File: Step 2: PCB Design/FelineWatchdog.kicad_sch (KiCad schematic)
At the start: 32 parts, among them J1 USB_C_Receptacle_PowerOnly_6P, J12 Conn_01x04_Socket, J2 Conn_01x02_Socket, J3 Conn_01x02_Pin, J9 USB_B_Micro, Q2 FS8205A, SW1 RESET, U1 AMS1117-3.3, U3 TP4056, U4 DW01A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

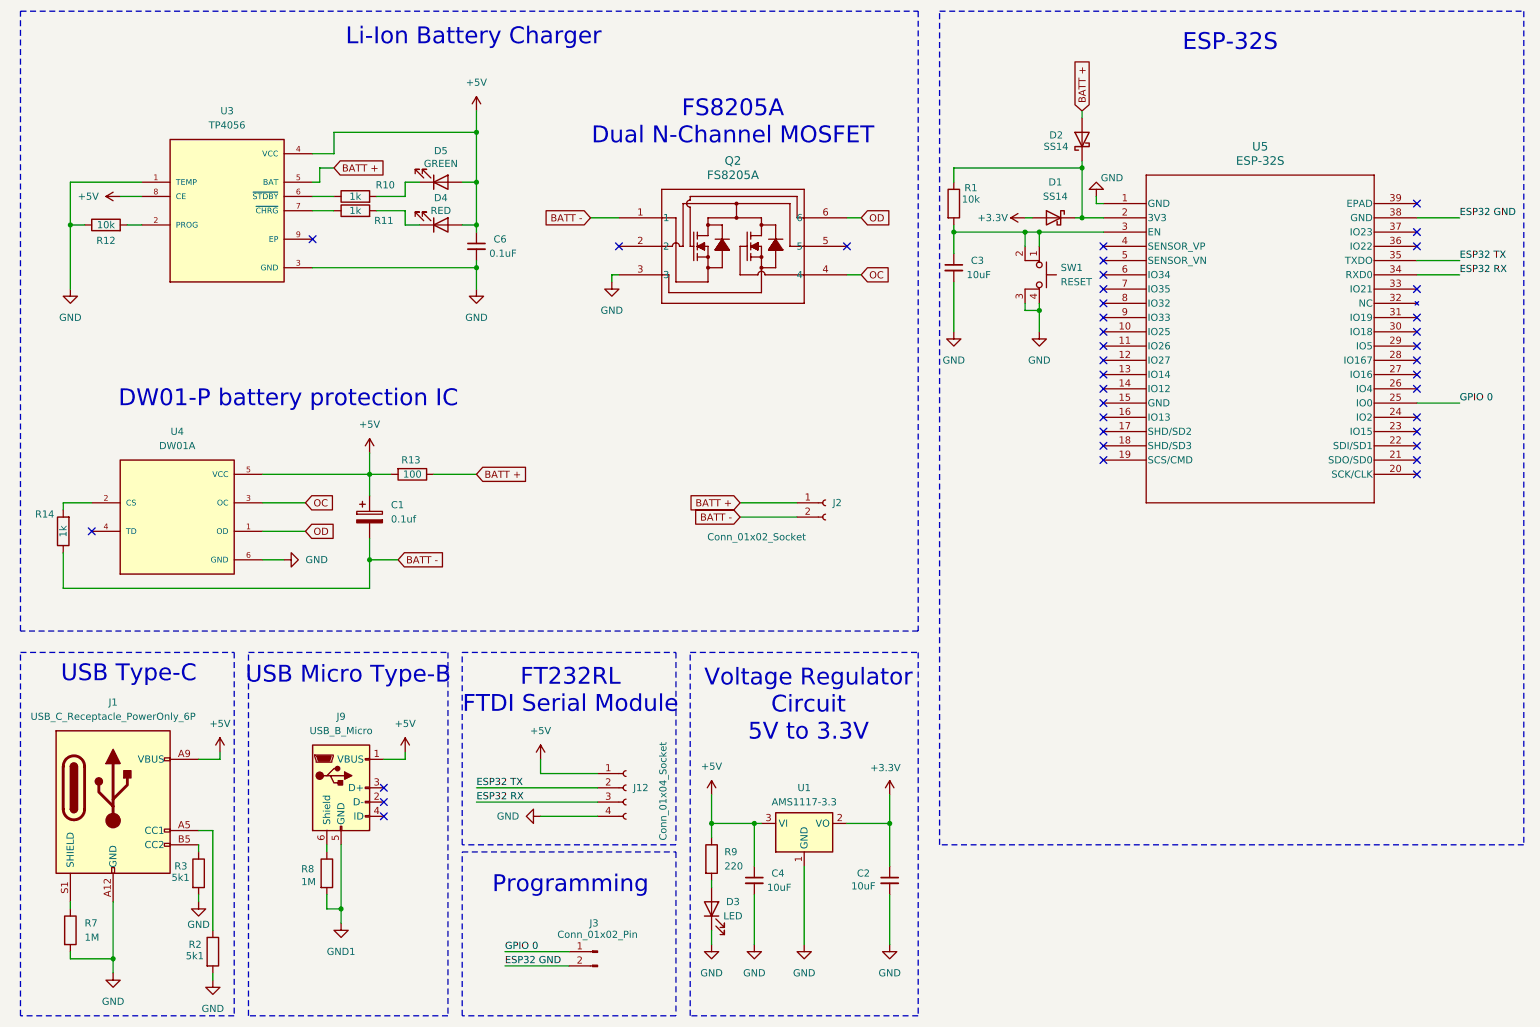
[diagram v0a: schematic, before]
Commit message: Switch to 4-layer PCB stackup with dedicated power and ground planes Inner layers ensure stable power delivery, improved signal integrity, and reduced EMI.
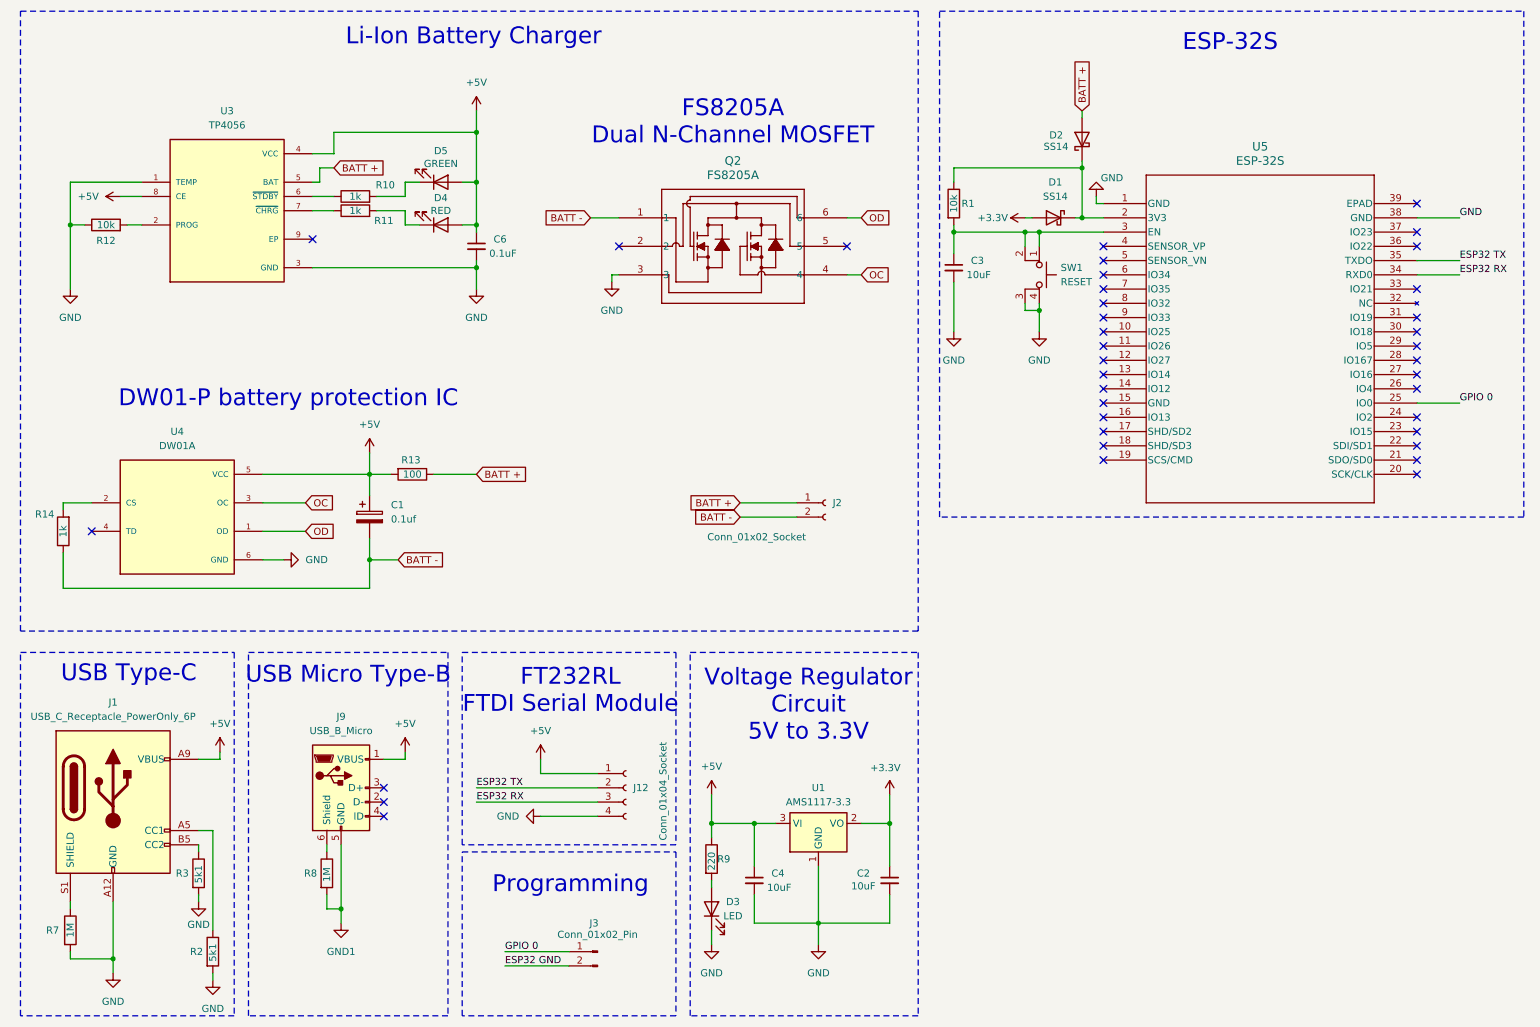
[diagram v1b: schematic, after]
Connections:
- net ESP32 GND: no longer U5.38 (GND)
- net GND: now also U5.38 (GND)
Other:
- moved on the sheet: U1
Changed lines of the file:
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@@
 	)
 	(junction
+		(at 156.21 177.8)
+		(diameter 0)
+		(color 0 0 0 0)
+	)
+	(junction
 		(at 30.48 184.15)
 		(diameter 0)
@@
 	(wire
 		(pts
+			(xy 168.91 172.72) (xy 168.91 177.8)
+		)
+		(stroke
+			(width 0)
+			(type default)
+		)
+	)
+	(wire
+		(pts
 			(xy 66.04 60.96) (xy 95.25 60.96)
 		)
@@
 	(wire
 		(pts
-			(xy 144.78 160.02) (xy 146.05 160.02)
+			(xy 144.78 160.02) (xy 148.59 160.02)
 		)
 		(stroke
@@
 	(wire
 		(pts
-			(xy 153.67 167.64) (xy 153.67 181.61)
+			(xy 156.21 167.64) (xy 156.21 177.8)
 		)
 		(stroke
@@
 	(wire
 		(pts
-			(xy 168.91 172.72) (xy 168.91 181.61)
+			(xy 156.21 177.8) (xy 168.91 177.8)
 		)
 		(stroke
@@
 	(wire
 		(pts
+			(xy 156.21 177.8) (xy 156.21 181.61)
+		)
+		(stroke
+			(width 0)
+			(type default)
+		)
+	)
+	(wire
+		(pts
+			(xy 144.78 172.72) (xy 144.78 177.8)
+		)
+		(stroke
+			(width 0)
+			(type default)
+		)
+	)
+	(wire
+		(pts
 			(xy 195.58 54.61) (xy 207.01 54.61)
 		)
@@
 	(wire
 		(pts
-			(xy 161.29 160.02) (xy 168.91 160.02)
+			(xy 163.83 160.02) (xy 168.91 160.02)
 		)
 		(stroke
@@
 	(wire
 		(pts
-			(xy 95.25 53.34) (xy 95.25 45.72)
+			(xy 144.78 177.8) (xy 156.21 177.8)
 		)
 		(stroke
@@
 	(wire
 		(pts
-			(xy 92.71 45.72) (xy 95.25 45.72)
+			(xy 95.25 53.34) (xy 95.25 45.72)
 		)
 		(stroke
@@
 	(wire
 		(pts
-			(xy 66.04 48.26) (xy 69.85 48.26)
+			(xy 92.71 45.72) (xy 95.25 45.72)
 		)
 		(stroke
@@
 	(wire
 		(pts
-			(xy 144.78 172.72) (xy 144.78 181.61)
+			(xy 66.04 48.26) (xy 69.85 48.26)
 		)
 		(stroke
@@
 	(rectangle
 		(start 177.8 15.24)
-		(end 281.94 163.83)
+		(end 281.94 105.41)
 		(stroke
 			(width 0)
@@
 		)
 	)
-	(label "ESP32 GND"
-		(at 270.51 52.07 0)
-		(fields_autoplaced yes)
-		(effects
-			(font
-				(size 1.27 1.27)
-			)
-			(justify left bottom)
-		)
-	)
 	(label "ESP32 TX"
 		(at 95.25 153.67 0)
@@
 		)
 	)
+	(label "GND"
+		(at 270.51 52.07 0)
+		(fields_autoplaced yes)
+		(effects
+			(font
+				(size 1.27 1.27)
+			)
+			(justify left bottom)
+		)
+	)
 	(global_label "BATT +"
 		(shape input)
@@
 		(on_board yes)
 		(dnp no)
-		(fields_autoplaced yes)
 		(property "Reference" "R7"
-			(at 25.4 177.7999 0)
+			(at 18.542 179.07 0)
 			(effects
 				(font
@@
 		)
 		(property "Value" "1M"
-			(at 25.4 180.3399 0)
+			(at 22.86 180.34 90)
 			(effects
 				(font
@@
 	(symbol
 		(lib_id "power:GND")
-		(at 153.67 181.61 0)
+		(at 156.21 181.61 0)
 		(unit 1)
 		(exclude_from_sim no)
@@
 		(fields_autoplaced yes)
 		(property "Reference" "#PWR012"
-			(at 153.67 187.96 0)
+			(at 156.21 187.96 0)
 			(effects
 				(font
@@
 		)
 		(property "Value" "GND"
-			(at 153.67 186.69 0)
+			(at 156.21 186.69 0)
 			(effects
 				(font
@@
 		)
 		(property "Footprint" ""
-			(at 153.67 181.61 0)
+			(at 156.21 181.61 0)
 			(effects
 				(font
@@
 		)
 		(property "Datasheet" ""
-			(at 153.67 181.61 0)
+			(at 156.21 181.61 0)
 			(effects
 				(font
@@
 		)
 		(property "Description" "Power symbol creates a global label with name \"GND\" , ground"
-			(at 153.67 181.61 0)
+			(at 156.21 181.61 0)
 			(effects
 				(font
@@
 	)
 	(symbol
-		(lib_id "power:GND")
-		(at 144.78 181.61 0)
-		(unit 1)
-		(exclude_from_sim no)
-		(in_bom yes)
-		(on_board yes)
-		(dnp no)
-		(fields_autoplaced yes)
-		(property "Reference" "#PWR011"
-			(at 144.78 187.96 0)
-			(effects
-				(font
-					(size 1.27 1.27)
-				)
-				(hide yes)
-			)
-		)
-		(property "Value" "GND"
-			(at 144.78 186.69 0)
-			(effects
-				(font
-					(size 1.27 1.27)
-				)
-			)
-		)
-		(property "Footprint" ""
-			(at 144.78 181.61 0)
-			(effects
-				(font
-					(size 1.27 1.27)
-				)
-				(hide yes)
-			)
-		)
-		(property "Datasheet" ""
-			(at 144.78 181.61 0)
-			(effects
-				(font
-					(size 1.27 1.27)
-				)
-				(hide yes)
-			)
-		)
-		(property "Description" "Power symbol creates a global label with name \"GND\" , ground"
-			(at 144.78 181.61 0)
-			(effects
-				(font
-					(size 1.27 1.27)
-				)
-				(hide yes)
-			)
-		)
-		(pin "1"
-		)
-		(instances
-			(project "FelineWatchdog"
-				(path "/8c4adf75-2d7a-4707-8808-772a211f889e"
-					(reference "#PWR011")
-					(unit 1)
-				)
-			)
-		)
-	)
-	(symbol
 		(lib_id "Device:R")
 		(at 73.66 48.26 90)
@@
 	(symbol
 		(lib_id "Regulator_Linear:AMS1117-3.3")
-		(at 153.67 160.02 0)
+		(at 156.21 160.02 0)
 		(unit 1)
 		(exclude_from_sim no)
@@
 		(fields_autoplaced yes)
 		(property "Reference" "U1"
-			(at 153.67 153.67 0)
+			(at 156.21 153.67 0)
 			(effects
 				(font
@@
 		)
 		(property "Value" "AMS1117-3.3"
-			(at 153.67 156.21 0)
+			(at 156.21 156.21 0)
 			(effects
 				(font
@@
 		)
 		(property "Footprint" "Package_TO_SOT_SMD:SOT-223-3_TabPin2"
-			(at 153.67 154.94 0)
+			(at 156.21 154.94 0)
 			(effects
 				(font
@@
 		)
 		(property "Datasheet" "http://www.advanced-monolithic.com/pdf/ds1117.pdf"
-			(at 156.21 166.37 0)
+			(at 158.75 166.37 0)
 			(effects
 				(font
@@
 		)
 		(property "Description" "1A Low Dropout regulator, positive, 3.3V fixed output, SOT-223"
-			(at 153.67 160.02 0)
+			(at 156.21 160.02 0)
 			(effects
 				(font
@@
 		(dnp no)
 		(property "Reference" "R2"
-			(at 43.942 181.61 0)
+			(at 44.196 182.88 0)
 			(effects
 				(font
@@
 		)
 		(property "Value" "5k1"
-			(at 43.434 183.642 0)
+			(at 48.26 184.658 90)
 			(effects
 				(font
@@
 		(dnp no)
 		(property "Reference" "R3"
-			(at 41.402 167.64 0)
+			(at 41.656 168.91 0)
 			(effects
 				(font
@@
 		)
 		(property "Value" "5k1"
-			(at 40.894 169.672 0)
+			(at 45.72 170.688 90)
 			(effects
 				(font
@@
 		(dnp no)
 		(property "Reference" "R9"
-			(at 139.446 165.1 0)
+			(at 138.176 166.37 0)
 			(effects
 				(font
@@
 		)
 		(property "Value" "220"
-			(at 139.446 167.64 0)
+			(at 137.16 168.402 90)
 			(effects
 				(font
@@
 	)
 	(symbol
-		(lib_id "power:GND")
-		(at 168.91 181.61 0)
-		(unit 1)
-		(exclude_from_sim no)
-		(in_bom yes)
-		(on_board yes)
-		(dnp no)
-		(fields_autoplaced yes)
-		(property "Reference" "#PWR025"
-			(at 168.91 187.96 0)
-			(effects
-				(font
-					(size 1.27 1.27)
-				)
-				(hide yes)
-			)
-		)
-		(property "Value" "GND"
-			(at 168.91 186.69 0)
-			(effects
-				(font
-					(size 1.27 1.27)
-				)
-			)
-		)
-		(property "Footprint" ""
-			(at 168.91 181.61 0)
-			(effects
-				(font
-					(size 1.27 1.27)
-				)
-				(hide yes)
-			)
-		)
-		(property "Datasheet" ""
-			(at 168.91 181.61 0)
-			(effects
-				(font
-					(size 1.27 1.27)
-				)
-				(hide yes)
-			)
-		)
-		(property "Description" "Power symbol creates a global label with name \"GND\" , ground"
-			(at 168.91 181.61 0)
-			(effects
-				(font
-					(size 1.27 1.27)
-				)
-				(hide yes)
-			)
-		)
-		(pin "1"
-		)
-		(instances
-			(project "FelineWatchdog"
-				(path "/8c4adf75-2d7a-4707-8808-772a211f889e"
-					(reference "#PWR025")
-					(unit 1)
-				)
-			)
-		)
-	)
-	(symbol
 		(lib_id "Connector:USB_C_Receptacle_PowerOnly_6P")
 		(at 30.48 156.21 0)
@@
 		(dnp no)
 		(property "Reference" "R1"
-			(at 183.388 46.736 0)
+			(at 182.88 49.53 0)
 			(effects
 				(font
@@
 		)
 		(property "Value" "10k"
-			(at 183.388 48.768 0)
+			(at 180.34 49.53 90)
 			(effects
 				(font
@@
 		(dnp no)
 		(property "Reference" "R8"
-			(at 64.008 168.148 0)
+			(at 64.516 168.91 0)
 			(effects
 				(font
@@
 		)
 		(property "Value" "1M"
-			(at 64.008 170.434 0)
+			(at 68.58 170.434 90)
 			(effects
 				(font
